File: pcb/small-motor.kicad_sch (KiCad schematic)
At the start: 27 parts, among them Q3 AON7544, Q4 AON7544, Q5 AON7544, Q6 AON7544, Q7 AON7544, Q8 AON7544, U7 DRV8323H

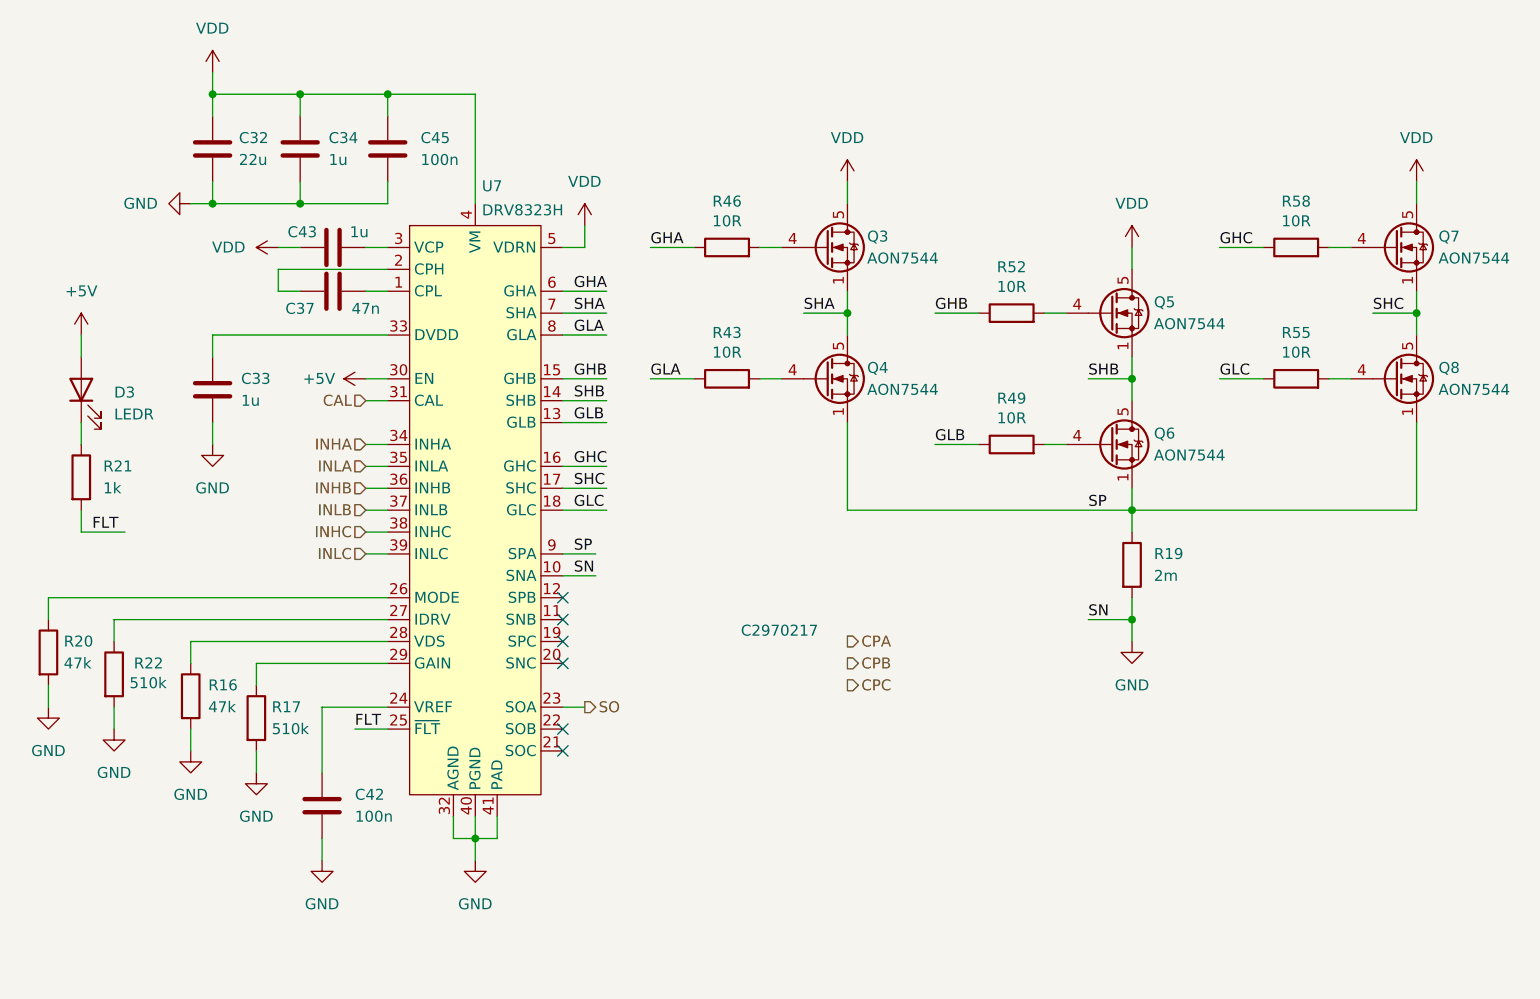
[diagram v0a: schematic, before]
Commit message: Finish rough layout
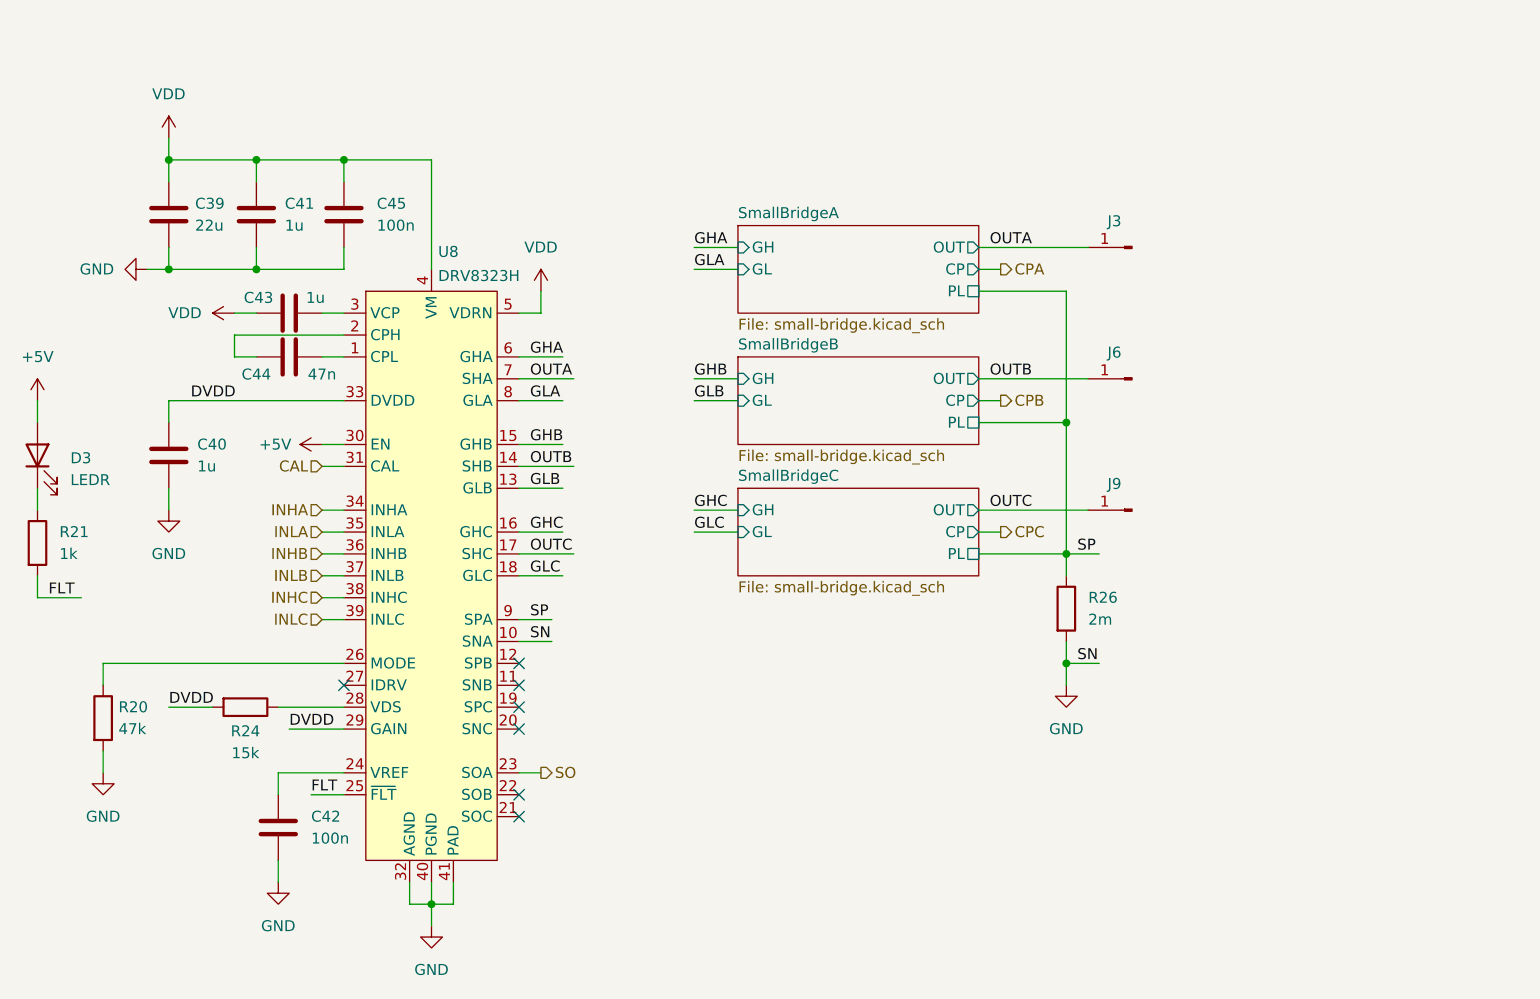
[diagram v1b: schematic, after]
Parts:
- removed Q3, Q4, Q5, Q6, Q7, Q8: AON7544, User_Footprints:DFN3x3A_8L_EP1_P, symbol User_Symbols:AON7544
- removed R16: 47k, Resistor_SMD:R_0402_1005Metric, symbol Device:R
- removed R17, R22: 510k, Resistor_SMD:R_0402_1005Metric, symbol Device:R
- removed R43, R46, R49, R52, R55, R58: 10R, Resistor_SMD:R_0402_1005Metric, symbol Device:R
- added J3, J6, J9: Conn_01x01_Pin, User_Footprints:Pad-P1.5, symbol Connector:Conn_01x01_Pin
- added R24: 15k, Resistor_SMD:R_0402_1005Metric, symbol Device:R
- C39: renamed from C32; footprint Resistor_SMD:R_0805_2012Metric -> Capacitor_SMD:C_0805_2012Metric
- C40: renamed from C33; footprint Resistor_SMD:R_0402_1005Metric -> Capacitor_SMD:C_0402_1005Metric
- C42: LCSC (none) -> C1525
- C43: footprint Resistor_SMD:R_0402_1005Metric -> Capacitor_SMD:C_0402_1005Metric
- C44: renamed from C37; LCSC (none) -> C1622
- C45: LCSC (none) -> C307331
- R20: LCSC (none) -> C25792
- renumbered C34 to C41, R19 to R26, U7 to U8
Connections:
- net DVDD: now reaches U8.29 (GAIN)
- net DVDD: now also C40.1, U8.33 (DVDD), R24.2
- net at U8.28 (VDS): now also R24.1
- net SHA renamed OUTA
- net OUTA: now also J3.1 (Pin_1)
- net SHB renamed OUTB
- net OUTB: now also J6.1 (Pin_1)
- net SHC renamed OUTC
- net OUTC: now also J9.1 (Pin_1)
- no-connect marks 6 -> 7
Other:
- added sheet SmallBridgeA (small-bridge.kicad_sch)
- added sheet SmallBridgeB (small-bridge.kicad_sch)
- added sheet SmallBridgeC (small-bridge.kicad_sch)
- note removed: "C2970217"
- moved on the sheet: C39, C40, C41, C42, C43, C44, C45, D3, R20, R21, R26, U8

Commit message: Save layout
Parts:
- renumbered J9 to J10, J3 to J4, J6 to J7
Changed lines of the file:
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@@
 		(on_board yes)
 		(dnp no)
-		(property "Reference" "J9"
+		(property "Reference" "J10"
 			(at 145.288 70.612 0)
 			(effects
@@
 		(on_board yes)
 		(dnp no)
-		(property "Reference" "J3"
+		(property "Reference" "J4"
 			(at 145.288 40.132 0)
 			(effects
@@
 		(on_board yes)
 		(dnp no)
-		(property "Reference" "J6"
+		(property "Reference" "J7"
 			(at 145.288 55.372 0)
 			(effects

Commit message: Save old buck regulator
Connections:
- net GHA: now also U8.16 (GHC); no longer U8.6 (GHA)
- net GHC: now also U8.6 (GHA); no longer U8.16 (GHC)
- net GLA: now also U8.18 (GLC); no longer U8.8 (GLA)
- net GLC: now also U8.8 (GLA); no longer U8.18 (GLC)
- net OUTA: now also U8.17 (SHC); no longer U8.7 (SHA)
- net OUTC: now also U8.7 (SHA); no longer U8.17 (SHC)
- net +3V3: now reaches C42.1, U8.24 (VREF)
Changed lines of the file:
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@@
 		(color 0 0 0 0)
 	)
+	(junction
+		(at 48.26 104.14)
+		(diameter 0)
+		(color 0 0 0 0)
+	)
 	(no_connect
 		(at 76.2 99.06)
@@
 	(wire
 		(pts
-			(xy 76.2 58.42) (xy 82.55 58.42)
+			(xy 76.2 78.74) (xy 82.55 78.74)
 		)
 		(stroke
@@
 	(wire
 		(pts
-			(xy 76.2 55.88) (xy 81.28 55.88)
+			(xy 76.2 76.2) (xy 81.28 76.2)
 		)
 		(stroke
@@
 	(wire
 		(pts
-			(xy 76.2 60.96) (xy 81.28 60.96)
+			(xy 76.2 81.28) (xy 81.28 81.28)
 		)
 		(stroke
@@
 	(wire
 		(pts
-			(xy 76.2 78.74) (xy 82.55 78.74)
+			(xy 76.2 58.42) (xy 82.55 58.42)
 		)
 		(stroke
@@
 	(wire
 		(pts
+			(xy 45.72 104.14) (xy 48.26 104.14)
+		)
+		(stroke
+			(width 0)
+			(type default)
+		)
+	)
+	(wire
+		(pts
 			(xy 129.54 58.42) (xy 142.24 58.42)
 		)
@@
 	(wire
 		(pts
-			(xy 76.2 76.2) (xy 81.28 76.2)
+			(xy 76.2 55.88) (xy 81.28 55.88)
 		)
 		(stroke
@@
 	(wire
 		(pts
-			(xy 45.72 45.72) (xy 55.88 45.72)
+			(xy 55.88 45.72) (xy 45.72 45.72)
 		)
 		(stroke
@@
 	(wire
 		(pts
-			(xy 76.2 81.28) (xy 81.28 81.28)
+			(xy 76.2 60.96) (xy 81.28 60.96)
 		)
 		(stroke
@@
 	)
 	(label "GHA"
-		(at 77.47 55.88 0)
+		(at 77.47 76.2 0)
 		(fields_autoplaced yes)
 		(effects
@@
 	)
 	(label "GHC"
-		(at 77.47 76.2 0)
+		(at 77.47 55.88 0)
 		(fields_autoplaced yes)
 		(effects
@@
 	)
 	(label "GLA"
-		(at 77.47 60.96 0)
+		(at 77.47 81.28 0)
 		(fields_autoplaced yes)
 		(effects
@@
 	)
 	(label "OUTA"
-		(at 77.47 58.42 0)
+		(at 77.47 78.74 0)
 		(fields_autoplaced yes)
 		(effects
@@
 	)
 	(label "GLC"
-		(at 77.47 81.28 0)
+		(at 77.47 60.96 0)
 		(fields_autoplaced yes)
 		(effects
@@
 	)
 	(label "OUTC"
-		(at 77.47 78.74 0)
+		(at 77.47 58.42 0)
 		(fields_autoplaced yes)
 		(effects
@@
 	)
 	(symbol
+		(lib_id "power:+3V3")
+		(at 45.72 104.14 90)
+		(unit 1)
+		(exclude_from_sim no)
+		(in_bom yes)
+		(on_board yes)
+		(dnp no)
+		(fields_autoplaced yes)
+		(property "Reference" "#PWR0144"
+			(at 49.53 104.14 0)
+			(effects
+				(font
+					(size 1.27 1.27)
+				)
+				(hide yes)
+			)
+		)
+		(property "Value" "+3V3"
+			(at 41.91 104.1399 90)
+			(effects
+				(font
+					(size 1.27 1.27)
+				)
+				(justify left)
+			)
+		)
+		(property "Footprint" ""
+			(at 45.72 104.14 0)
+			(effects
+				(font
+					(size 1.27 1.27)
+				)
+				(hide yes)
+			)
+		)
+		(property "Datasheet" ""
+			(at 45.72 104.14 0)
+			(effects
+				(font
+					(size 1.27 1.27)
+				)
+				(hide yes)
+			)
+		)
+		(property "Description" "Power symbol creates a global label with name \"+3V3\""
+			(at 45.72 104.14 0)
+			(effects
+				(font
+					(size 1.27 1.27)
+				)
+				(hide yes)
+			)
+		)
+		(pin "1"
+		)
+		(instances
+			(project ""
+				(path "/38b0a34b-2047-47f6-90d7-ccdf77e8e212/32afc7a0-18ac-478c-98c2-4feaa662b50f"
+					(reference "#PWR0145")
+					(unit 1)
+				)
+				(path "/38b0a34b-2047-47f6-90d7-ccdf77e8e212/48688cd5-574e-41ae-9494-1d572dc1abc1"
+					(reference "#PWR0146")
+					(unit 1)
+				)
+				(path "/38b0a34b-2047-47f6-90d7-ccdf77e8e212/cb19eb0b-a3a9-419c-b6d9-e67d0e4f95b4"
+					(reference "#PWR0144")
+					(unit 1)
+				)
+			)
+		)
+	)
+	(symbol
 		(lib_id "power:VDD")
 		(at 78.74 48.26 0)
@@
 	)
 	(sheet
-		(at 101.6 55.88)
+		(at 101.6 71.12)
 		(size 27.94 10.16)
 		(fields_autoplaced yes)
@@
 			(color 0 0 0 0.0000)
 		)
-		(property "Sheetname" "SmallBridgeB"
-			(at 101.6 55.1684 0)
+		(property "Sheetname" "SmallBridgeC"
+			(at 101.6 70.4084 0)
 			(effects
 				(font
@@
 		)
 		(property "Sheetfile" "small-bridge.kicad_sch"
-			(at 101.6 66.6246 0)
+			(at 101.6 81.8646 0)
 			(effects
 				(font
@@
 		)
 		(pin "GL" input
-			(at 101.6 60.96 180)
+			(at 101.6 76.2 180)
 			(effects
 				(font
@@
 		)
 		(pin "PL" passive
-			(at 129.54 63.5 0)
+			(at 129.54 78.74 0)
 			(effects
 				(font
@@
 		)
 		(pin "OUT" output
-			(at 129.54 58.42 0)
+			(at 129.54 73.66 0)
 			(effects
 				(font
@@
 		)
 		(pin "GH" input
-			(at 101.6 58.42 180)
+			(at 101.6 73.66 180)
 			(effects
 				(font
@@
 		)
 		(pin "CP" output
-			(at 129.54 60.96 0)
+			(at 129.54 76.2 0)
 			(effects
 				(font
@@
 	)
 	(sheet
-		(at 101.6 71.12)
+		(at 101.6 40.64)
 		(size 27.94 10.16)
 		(fields_autoplaced yes)
@@
 			(color 0 0 0 0.0000)
 		)
-		(property "Sheetname" "SmallBridgeC"
-			(at 101.6 70.4084 0)
+		(property "Sheetname" "SmallBridgeA"
+			(at 101.6 39.9284 0)
 			(effects
 				(font
@@
 		)
 		(property "Sheetfile" "small-bridge.kicad_sch"
-			(at 101.6 81.8646 0)
+			(at 101.6 51.3846 0)
 			(effects
 				(font
@@
 		)
 		(pin "GL" input
-			(at 101.6 76.2 180)
+			(at 101.6 45.72 180)
 			(effects
 				(font
@@
 		)
 		(pin "PL" passive
-			(at 129.54 78.74 0)
+			(at 129.54 48.26 0)
 			(effects
 				(font
@@
 		)
 		(pin "OUT" output
-			(at 129.54 73.66 0)
+			(at 129.54 43.18 0)
 			(effects
 				(font
@@
 		)
 		(pin "GH" input
-			(at 101.6 73.66 180)
+			(at 101.6 43.18 180)
 			(effects
 				(font
@@
 		)
 		(pin "CP" output
-			(at 129.54 76.2 0)
+			(at 129.54 45.72 0)
 			(effects
 				(font
@@
 	)
 	(sheet
-		(at 101.6 40.64)
+		(at 101.6 55.88)
 		(size 27.94 10.16)
 		(fields_autoplaced yes)
@@
 			(color 0 0 0 0.0000)
 		)
-		(property "Sheetname" "SmallBridgeA"
-			(at 101.6 39.9284 0)
+		(property "Sheetname" "SmallBridgeB"
+			(at 101.6 55.1684 0)
 			(effects
 				(font
@@
 		)
 		(property "Sheetfile" "small-bridge.kicad_sch"
-			(at 101.6 51.3846 0)
+			(at 101.6 66.6246 0)
 			(effects
 				(font
@@
 		)
 		(pin "GL" input
-			(at 101.6 45.72 180)
+			(at 101.6 60.96 180)
 			(effects
 				(font
@@
 		)
 		(pin "PL" passive
-			(at 129.54 48.26 0)
+			(at 129.54 63.5 0)
 			(effects
 				(font
@@
 		)
 		(pin "OUT" output
-			(at 129.54 43.18 0)
+			(at 129.54 58.42 0)
 			(effects
 				(font
@@
 		)
 		(pin "GH" input
-			(at 101.6 43.18 180)
+			(at 101.6 58.42 180)
 			(effects
 				(font
@@
 		)
 		(pin "CP" output
-			(at 129.54 45.72 0)
+			(at 129.54 60.96 0)
 			(effects
 				(font

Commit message: Finish pcb
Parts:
- C44: footprint Capacitor_SMD:C_0402_1005Metric -> Capacitor_SMD:C_0603_1608Metric
- J10, J4, J7: now not fitted
- R21: LCSC (none) -> C11702
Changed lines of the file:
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@@
 		(dnp no)
 		(fields_autoplaced yes)
-		(property "Reference" "#PWR0144"
+		(property "Reference" "#PWR0145"
 			(at 49.53 104.14 0)
 			(effects
@@
 			)
 		)
-		(property "Footprint" "Capacitor_SMD:C_0402_1005Metric"
+		(property "Footprint" "Capacitor_SMD:C_0603_1608Metric"
 			(at 53.34 54.9148 0)
 			(effects
@@
 			)
 		)
+		(property "LCSC" "C11702"
+			(at 20.32 77.47 0)
+			(effects
+				(font
+					(size 1.27 1.27)
+				)
+				(hide yes)
+			)
+		)
 		(pin "1"
 		)
@@
 		(in_bom no)
 		(on_board yes)
-		(dnp no)
+		(dnp yes)
 		(property "Reference" "J10"
 			(at 145.288 70.612 0)
@@
 		(in_bom no)
 		(on_board yes)
-		(dnp no)
+		(dnp yes)
 		(property "Reference" "J4"
 			(at 145.288 40.132 0)
@@
 		(in_bom no)
 		(on_board yes)
-		(dnp no)
+		(dnp yes)
 		(property "Reference" "J7"
 			(at 145.288 55.372 0)
